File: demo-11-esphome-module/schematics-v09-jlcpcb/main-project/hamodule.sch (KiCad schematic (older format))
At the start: 63 parts, among them J1 1017505, J2 Conn-ESP-Relays, J3 1017505, J4 Conn-Buttons, J5 Conn_01x02, J6 Conn-Esp-Sensors, J7 Conn-LedIndicators, J8 1017505, J9 Current Jumper, K1 G5Q-1, K2 G5Q-1, K3 G5Q-1, K4 G5Q-1, U1 ULN2003A, U2 LD1117S33TR_SOT223, U3 HCPL3700, U4 HCPL3700, U5 HCPL3700, U6 HCPL3700

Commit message: jlcpcb v2: increas connectors pads + fix numbering for sensors in labels
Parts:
- J1, J3, J8: footprint Phoenix_Conn:1017505 -> 1017505_updated_pretty:1017505_pretty
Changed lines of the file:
@@
 F 0 "J8" H 10800 1085 50  0000 C CNN
 F 1 "1017505" H 10800 1176 50  0000 C CNN
-F 2 "Phoenix_Conn:1017505" H 11050 1750 50  0001 L CNN
+F 2 "1017505_updated_pretty:1017505_pretty" H 11050 1750 50  0001 L CNN
 F 3 "https://www.phoenixcontact.com/online/portal/gb/?uri=pxc-oc-itemdetail:pid=1017505&library=gben&pcck=P-11-01-05&tab=1&selectedCategory=ALL" H 11050 1650 50  0001 L CNN
 F 4 "Phoenix Contact TDPT Series 5.08mm Pitch, PCB Terminal Block, PCB Mount, 4 Way" H 11050 1550 50  0001 L CNN "Description"
@@
 F 0 "J1" H 2300 635 50  0000 C CNN
 F 1 "1017505" H 2300 726 50  0000 C CNN
-F 2 "Phoenix_Conn:1017505" H 2550 1300 50  0001 L CNN
+F 2 "1017505_updated_pretty:1017505_pretty" H 2550 1300 50  0001 L CNN
 F 3 "https://www.phoenixcontact.com/online/portal/gb/?uri=pxc-oc-itemdetail:pid=1017505&library=gben&pcck=P-11-01-05&tab=1&selectedCategory=ALL" H 2550 1200 50  0001 L CNN
 F 4 "Phoenix Contact TDPT Series 5.08mm Pitch, PCB Terminal Block, PCB Mount, 4 Way" H 2550 1100 50  0001 L CNN "Description"
@@
 F 0 "J3" H 4500 735 50  0000 C CNN
 F 1 "1017505" H 4500 826 50  0000 C CNN
-F 2 "Phoenix_Conn:1017505" H 4750 1400 50  0001 L CNN
+F 2 "1017505_updated_pretty:1017505_pretty" H 4750 1400 50  0001 L CNN
 F 3 "https://www.phoenixcontact.com/online/portal/gb/?uri=pxc-oc-itemdetail:pid=1017505&library=gben&pcck=P-11-01-05&tab=1&selectedCategory=ALL" H 4750 1300 50  0001 L CNN
 F 4 "Phoenix Contact TDPT Series 5.08mm Pitch, PCB Terminal Block, PCB Mount, 4 Way" H 4750 1200 50  0001 L CNN "Description"

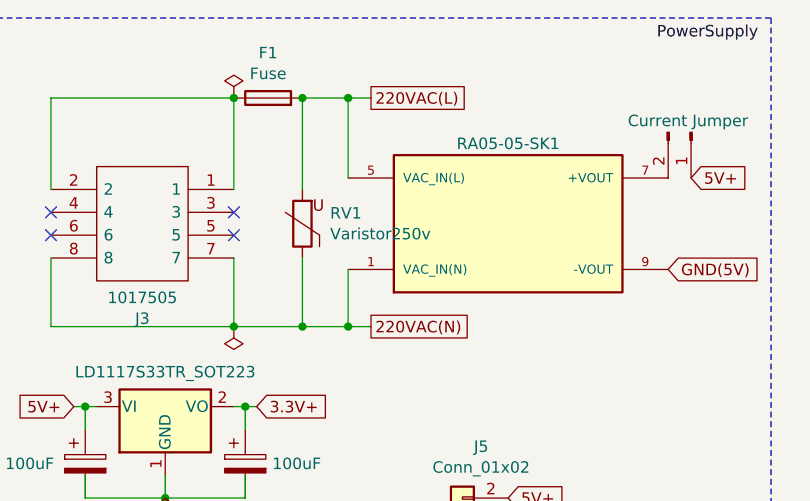
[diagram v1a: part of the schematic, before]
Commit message: adding an output fuse
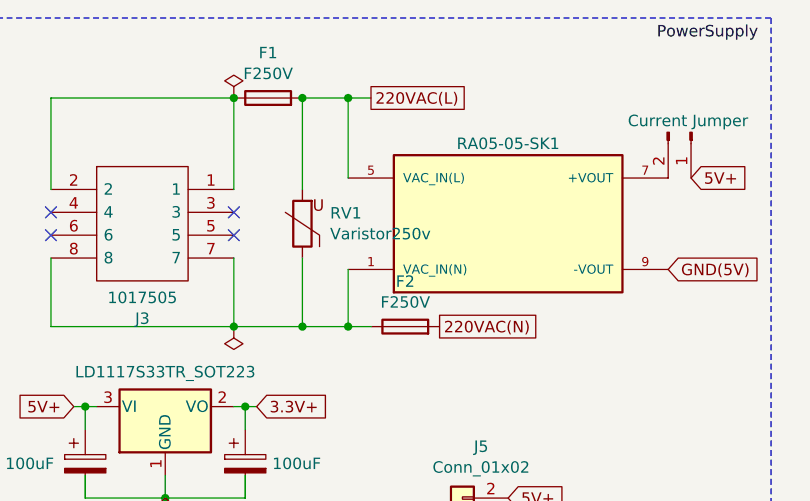
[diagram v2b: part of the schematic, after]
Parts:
- added F2: F250V, Fuse:Fuse_Littelfuse_372_D8.50mm, symbol Device:Fuse
- 22uF1, 22uF2, 22uF3, 22uF4: footprint Capacitor_THT:CP_Radial_D10.0mm_P5.00mm -> Capacitor_THT:CP_Radial_D5.0mm_P2.00mm
- F1: value Fuse -> F250V
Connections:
- net 220VAC(N): now also F2.2; no longer J3.7, J3.8, RA05-05-SK1.1 (VAC_IN(N)), RV1.1
- new net: F2.1, J3.7, J3.8, RA05-05-SK1.1 (VAC_IN(N)), RV1.1
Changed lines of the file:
@@
 F 0 "22uF1" H 9912 2454 50  0000 R CNN
 F 1 "CP_Small" H 9912 2545 50  0000 R CNN
-F 2 "Capacitor_THT:CP_Radial_D10.0mm_P5.00mm" H 10000 2500 50  0001 C CNN
+F 2 "Capacitor_THT:CP_Radial_D5.0mm_P2.00mm" H 10000 2500 50  0001 C CNN
 F 3 "~" H 10000 2500 50  0001 C CNN
 	1    10000 2500
@@
 F 0 "22uF2" H 9912 3454 50  0000 R CNN
 F 1 "CP_Small" H 9912 3545 50  0000 R CNN
-F 2 "Capacitor_THT:CP_Radial_D10.0mm_P5.00mm" H 10000 3500 50  0001 C CNN
+F 2 "Capacitor_THT:CP_Radial_D5.0mm_P2.00mm" H 10000 3500 50  0001 C CNN
 F 3 "~" H 10000 3500 50  0001 C CNN
 	1    10000 3500
@@
 F 0 "22uF3" H 9912 4454 50  0000 R CNN
 F 1 "CP_Small" H 9912 4545 50  0000 R CNN
-F 2 "Capacitor_THT:CP_Radial_D10.0mm_P5.00mm" H 10000 4500 50  0001 C CNN
+F 2 "Capacitor_THT:CP_Radial_D5.0mm_P2.00mm" H 10000 4500 50  0001 C CNN
 F 3 "~" H 10000 4500 50  0001 C CNN
 	1    10000 4500
@@
 F 0 "22uF4" H 9912 5454 50  0000 R CNN
 F 1 "CP_Small" H 9912 5545 50  0000 R CNN
-F 2 "Capacitor_THT:CP_Radial_D10.0mm_P5.00mm" H 10000 5500 50  0001 C CNN
+F 2 "Capacitor_THT:CP_Radial_D5.0mm_P2.00mm" H 10000 5500 50  0001 C CNN
 F 3 "~" H 10000 5500 50  0001 C CNN
 	1    10000 5500
@@
 P 5050 900
 F 0 "F1" V 5247 900 50  0000 C CNN
-F 1 "Fuse" V 5156 900 50  0000 C CNN
+F 1 "F250V" V 5156 900 50  0000 C CNN
 F 2 "Fuse:Fuse_Littelfuse_372_D8.50mm" V 4980 900 50  0001 C CNN
 F 3 "~" H 5050 900 50  0001 C CNN
@@
 Text GLabel 6800 1650 2    50   Input ~ 0
 GND(5V)
-Text GLabel 5500 1900 2    50   UnSpc ~ 0
+Text GLabel 5800 1900 2    50   UnSpc ~ 0
 220VAC(N)
 Wire Wire Line
@@
 Wire Notes Line
 	3800 3050 7250 3050
+$Comp
+L Device:Fuse F2
+U 1 1 615EC85F
+P 5650 1900
+F 0 "F2" V 5847 1900 50  0000 C CNN
+F 1 "F250V" V 5756 1900 50  0000 C CNN
+F 2 "Fuse:Fuse_Littelfuse_372_D8.50mm" V 5580 1900 50  0001 C CNN
+F 3 "~" H 5650 1900 50  0001 C CNN
+	1    5650 1900
+	0    -1   -1   0
+$EndComp
 $EndSCHEMATC
